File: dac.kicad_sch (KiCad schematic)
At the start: 14 parts, among them J1 USB_C_Receptacle_USB2.0_16P, SW1 SW_Push, SW2 SW_Push, U1 USBLC6-2SC6, U2 CS43131, U3 TLV75518PDBV, U4 ESP32-S3-MINI-1U

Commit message: updt
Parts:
- removed C1, C2: 1uF, symbol Device:C_Small_US
- added C1, C11: 15uF, symbol Device:C_Small
- added C10, C8: 4.7uF, symbol Device:C_Small
- added C12, C13, C14: 2.2uF, symbol Device:C_Small
- added C2, C5, C6, C7: 1uF, symbol Device:C_Small
- added C3, C4, C9: 0.1uF, symbol Device:C_Small
- added J2: AudioJack3, symbol Connector_Audio:AudioJack3
- added R4: 6.7kR, symbol Device:R_Small_US
- added SW3: SW_Push, symbol Switch:SW_Push
- added U5: TLV75533PDBV, Package_TO_SOT_SMD:SOT-23-5, symbol Regulator_Linear:TLV75533PDBV
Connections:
- net +1V8: now also U2.31 (VL), U2.4 (VD), U2.7 (VA), C1.2, C12.2, C2.1, C3.1, C4.1
- net GND: now also U4.3 (3V3), C10.2, C12.1, C13.1, C2.2, C3.2, C4.2, C5.2, C6.2, C7.2, C8.1, C8.2, C9.2, J2.S, U5.2 (GND)
- net at U2.10 (FLYP_VA): now also C14.2
- net at U2.11 (FLYN_VA): now also C14.1
- net at U2.14 (HPOUTA): now also J2.R
- net at U2.16 (HPOUTB): now also J2.T
- net +3V3: now reaches U2.26 (VP)
- net +3V3: now also C10.1, C7.1, C9.1, R4.1, U5.5 (OUT)
- net EP_(GNDA): now reaches U2.41 (EP_(GNDA))
- net EP_(GNDA): now also U2.8 (GNDA)
- net at U2.5 (FILT+): now also C1.1
- net at U2.6 (FILT-): now also C11.2
- net at U2.9 (-VA): now also C11.1, C13.2
- net at F1.1, U3.1 (IN), U3.3 (EN): now also C5.1, C6.1, U5.1 (IN), U5.3 (EN)
- net RESET: now reaches U4.13 (IO9)
- net SDA: now reaches U4.16 (IO12)
- net SCL: now reaches U4.17 (IO13)
- net at U4.35 (IO39): now also R4.2, SW3.1
- net MCLK: now reaches U4.6 (IO2)
- net SCLK: now reaches U4.7 (IO3)
- net LRCK: now reaches U4.8 (IO4)
- net SDIN: now reaches U4.9 (IO5)
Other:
- moved on the sheet: D1, F1, J1, R1, R2, R3, SW1, SW2, U1, U3, U4

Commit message: updt
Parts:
- removed J2: AudioJack3, symbol Connector_Audio:AudioJack3
- added J2: AudioJack3_HPDetect, symbol dac:AudioJack3_HPDetect
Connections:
- net GND: now also U2.13 (HPREFA), U2.17 (HPREFB), J2.S
- net at U2.14 (HPOUTA): now also J2.R
- net at U2.16 (HPOUTB): now also J2.T
- net HP_DET: now reaches U2.22 (HP_DETECT)
- net HP_DET: now also J2.DET

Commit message: updt
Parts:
- added C15, C16, C17, C18, C19: 2.2uF, symbol Device:C_Small
- added R5, R6: 1kR, symbol Device:R_Small_US
- added U6: TLV75518PDBV, Package_TO_SOT_SMD:SOT-23-5, symbol Regulator_Linear:TLV75518PDBV
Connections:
- net GND is gone; now on net EP_(GNDA): C10.2, C12.1, C13.1, C2.2, C3.2, C4.2, C5.2, C6.2, C7.2, C8.1, C8.2, C9.2, D1.1 (K), J1.A1 (GND), J1.A12 (GND), J1.B1 (GND), J1.B12 (GND), J1.SH (SHIELD), J2.S, R1.2, R2.2, SW1.2, SW2.2, U1.2 (GND), U2.13 (HPREFA), U2.17 (HPREFB), U3.2 (GND), U4.1 (GND), U4.2 (GND), U4.3 (3V3), U4.42 (GND), U4.43 (GND), U4.46 (GND), U4.47 (GND), U4.48 (GND), U4.49 (GND), U4.50 (GND), U4.51 (GND), U4.52 (GND), U4.53 (GND), U4.54 (GND), U4.55 (GND), U4.56 (GND), U4.57 (GND), U4.58 (GND), U4.59 (GND), U4.60 (GND), U4.61 (GND), U4.62 (GND), U4.63 (GND), U4.64 (GND), U4.65 (GND), U5.2 (GND)
- net SDA is gone; now on net SCL: U4.16 (IO12)
- net +1V8: now also U2.25 (VCP), C17.2
- net +3V3: now also R5.1, R6.1
- net EP_(GNDA): now also U2.19 (GNDCP), U2.35 (GNDD), C15.2, C16.1, C17.1
- net RESET: now also U2.28 (RESET)
- net SCL: now also U2.1 (SCL), U2.39 (SDA), R5.2, R6.2
- net at J2.R, U2.14 (HPOUTA): now also J2.T, U2.16 (HPOUTB)
- net at U2.18 (VCP_FILT-): now also C15.1
- net at U2.20 (FLYN_VCP): now also C19.1
- net at U2.21 (VCP_FILT+): now also C16.2
- net at U2.23 (FLYC_VCP): now also C18.1, C19.2
- no-connect marks 0 -> 6
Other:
- moved on the sheet: C3, C4, C6, C7, J2, U5

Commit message: upgrade decoupling to 1k micro farads
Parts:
- removed U6: TLV75518PDBV, Package_TO_SOT_SMD:SOT-23-5, symbol Regulator_Linear:TLV75518PDBV
- added R7, R8: 4.7kR, symbol Device:R_Small_US
- added U6: PCA9306, symbol Interface:PCA9306
- C10: value 4.7uF -> 1uF
- C3, C4, C9: value 0.1uF -> 1uF
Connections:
- net +1V8: now also R8.1
- net +3V3: now also R7.1
- net EP_(GNDA): now also U6.1 (GND)
- new net: R7.2, U6.2 (VREF1)
- new net: R8.2, U6.7 (VREF2)

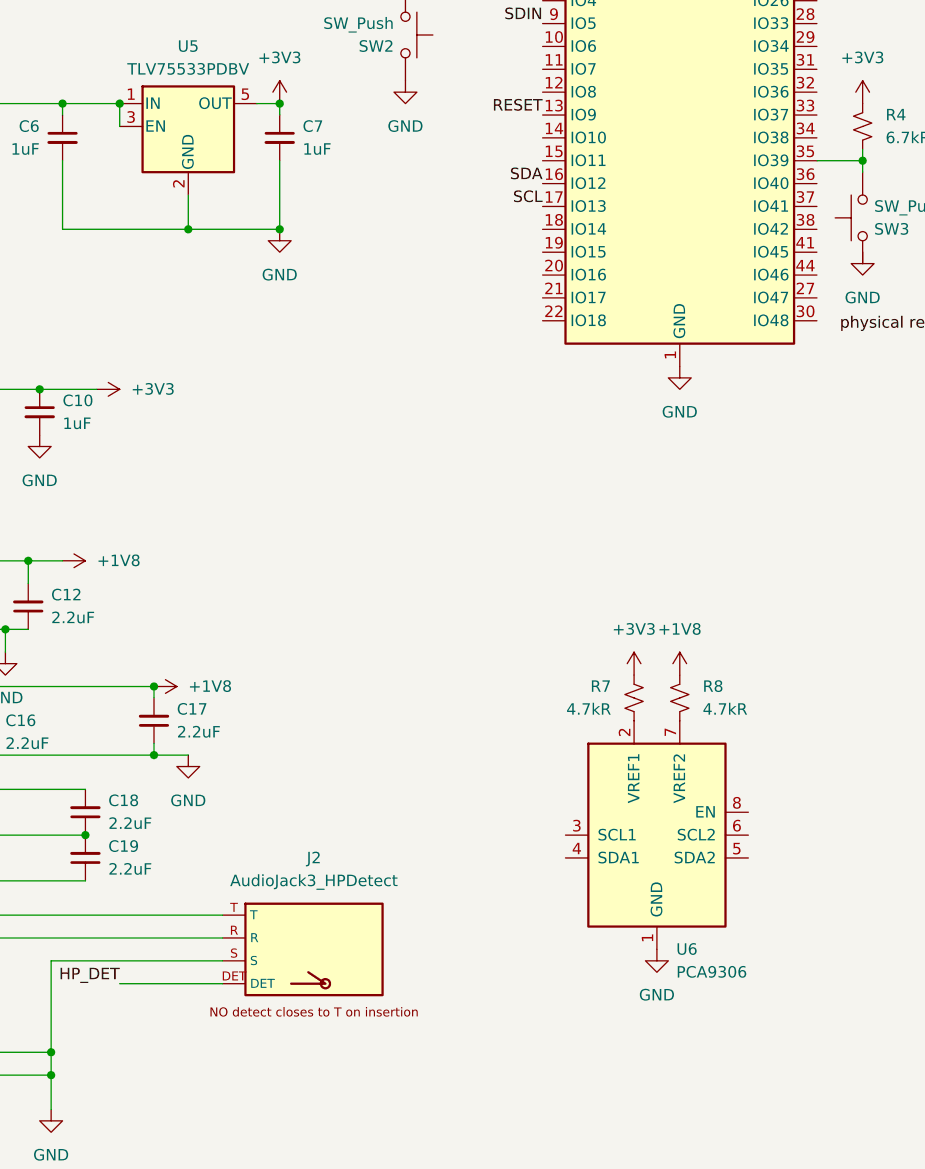
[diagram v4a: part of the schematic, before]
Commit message: add pca9306
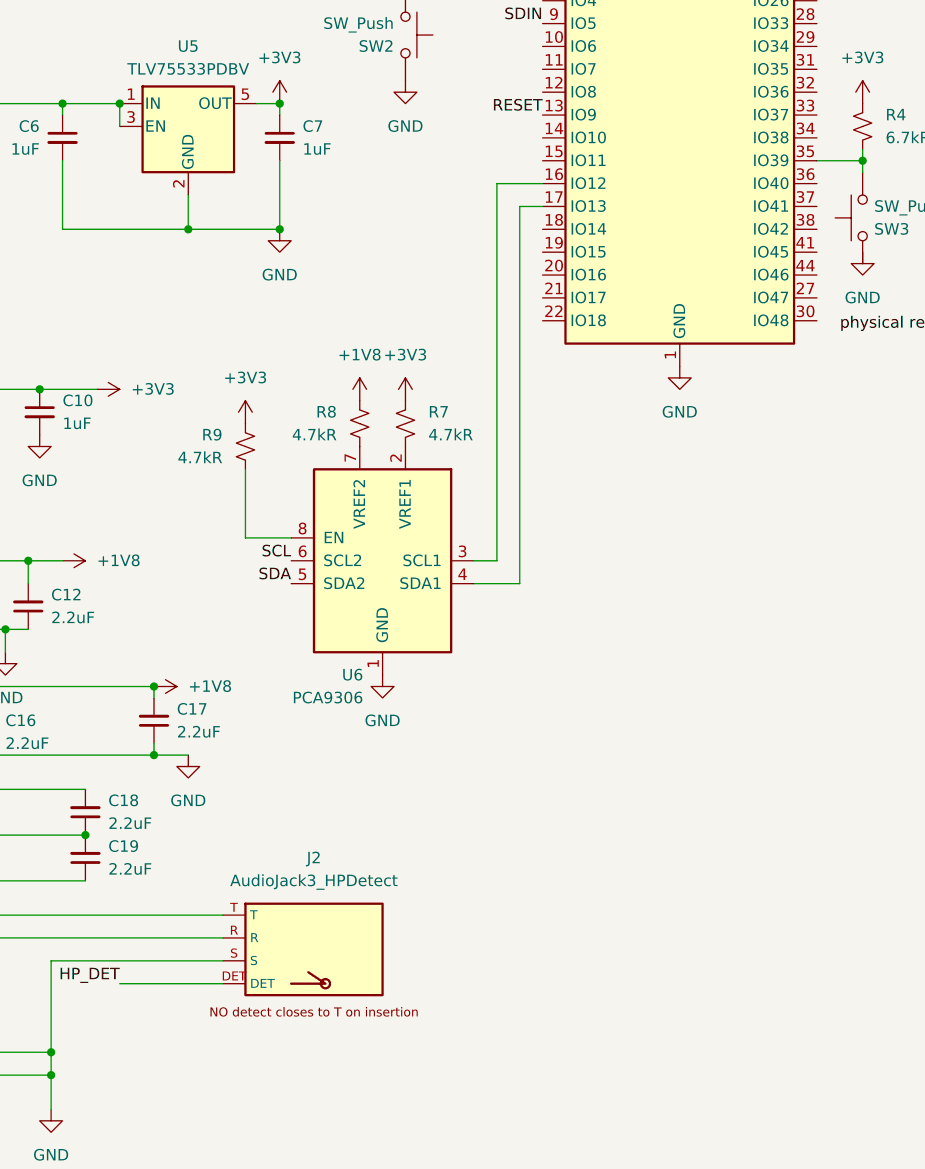
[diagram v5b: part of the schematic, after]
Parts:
- added R9: 4.7kR, symbol Device:R_Small_US
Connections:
- net +3V3: now also R9.1
- net SCL: now also U6.5 (SDA2), U6.6 (SCL2); no longer U4.16 (IO12), U4.17 (IO13)
- net at U6.3 (SCL1): now also U4.16 (IO12)
- net at U6.4 (SDA1): now also U4.17 (IO13)
- net at U6.8 (EN): now also R9.2
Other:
- moved on the sheet: R7, R8, U6

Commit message: ADD I2S 3V3 -> 1V8 IC THINGY WOW
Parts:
- added R10, R11, R12, R13, R14, R15, R16, R17, R18: 4.7kR, symbol Device:R_Small_US
- added U7, U8, U9: SN74LVC1T45DBV, Package_TO_SOT_SMD:SOT-23-6, symbol Logic_LevelTranslator:SN74LVC1T45DBV
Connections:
- net +1V8: now also R10.1, R13.1, R15.1
- net +3V3: now also R11.1, R12.1, R14.1, R16.1, R17.1, R18.1
- net EP_(GNDA): now also U2.30 (ADR), U7.2 (GND), U8.2 (GND), U9.2 (GND)
- net LRCK: now also U7.3 (A)
- net SCLK: now also U9.3 (A)
- net SDIN: now also U8.3 (A)
- net SDIN1: now reaches U2.2 (SDIN1)
- net SDIN1: now also U8.4 (B)
- net SCLK1: now reaches U2.34 (SCLK1)
- net SCLK1: now also U9.4 (B)
- net LRCK1: now reaches U2.38 (LRCK1)
- net LRCK1: now also U7.4 (B)
- net MCLK: no longer names the net of U4.6 (IO2)
- new net: R12.2, U8.1 (VCCA)
- new net: R13.2, U8.6 (VCCB)
- new net: R14.2, U9.1 (VCCA)
- new net: R11.2, U7.1 (VCCA)
- new net: R15.2, U9.6 (VCCB)
- new net: R17.2, U9.5 (DIR)
- new net: R16.2, U7.5 (DIR)
- new net: R10.2, U7.6 (VCCB)
